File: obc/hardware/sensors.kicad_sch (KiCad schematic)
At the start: 6 parts, among them J5 Conn_Coaxial, U4 MAX-M10S, U6 MS5607-02BA

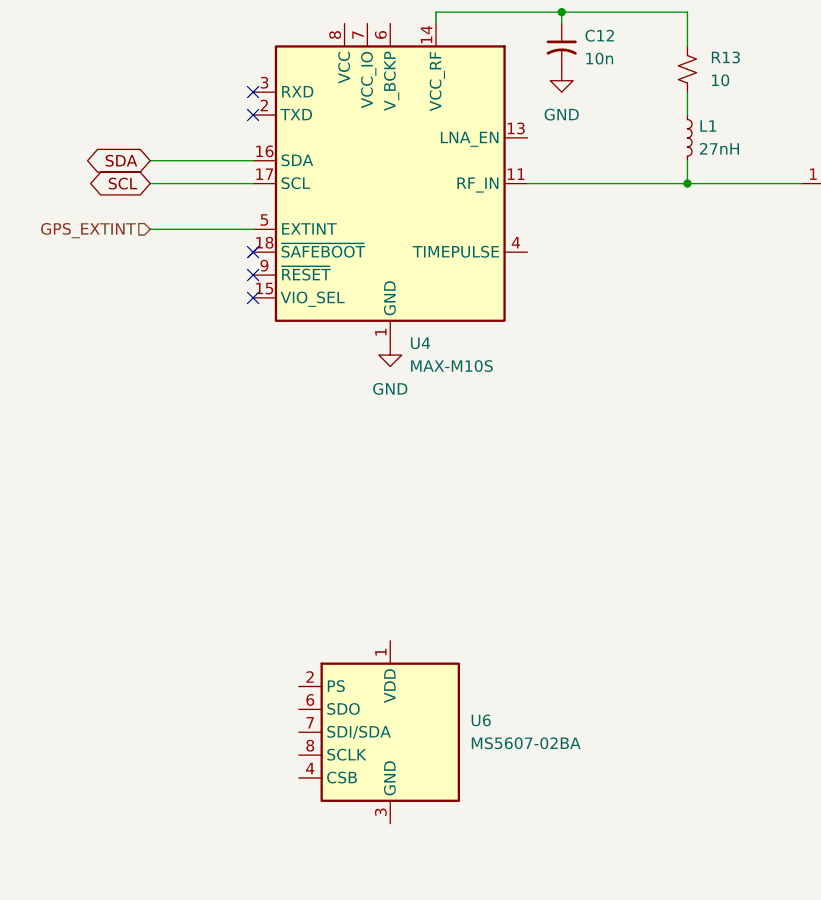
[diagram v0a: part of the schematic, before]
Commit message: added CAN, UART, supervisor, USB, power OR-ing, GPS, did layout
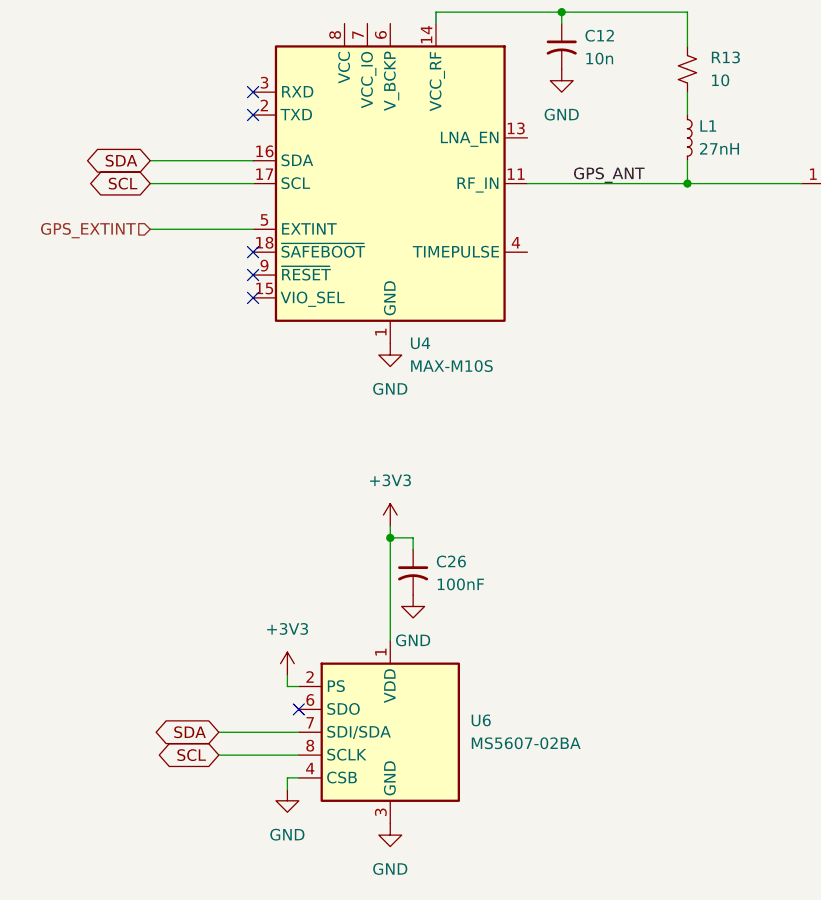
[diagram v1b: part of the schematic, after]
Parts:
- added C26: 100nF, Capacitor_SMD:C_0402_1005Metric, symbol Device:C_Small_US
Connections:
- net GND: now also U6.3 (GND), U6.4 (CSB), U6.5 (CSB), C26.2
- net SCL: now also U6.8 (SCLK)
- net SDA: now also U6.7 (SDI/SDA)
- net GPS_ANT: now reaches J5.1 (In), L1.2, U4.11 (RF_IN)
- net +3V3: now reaches U6.1 (VDD)
- net +3V3: now also U6.2 (PS), C26.1
- no-connect marks 5 -> 6

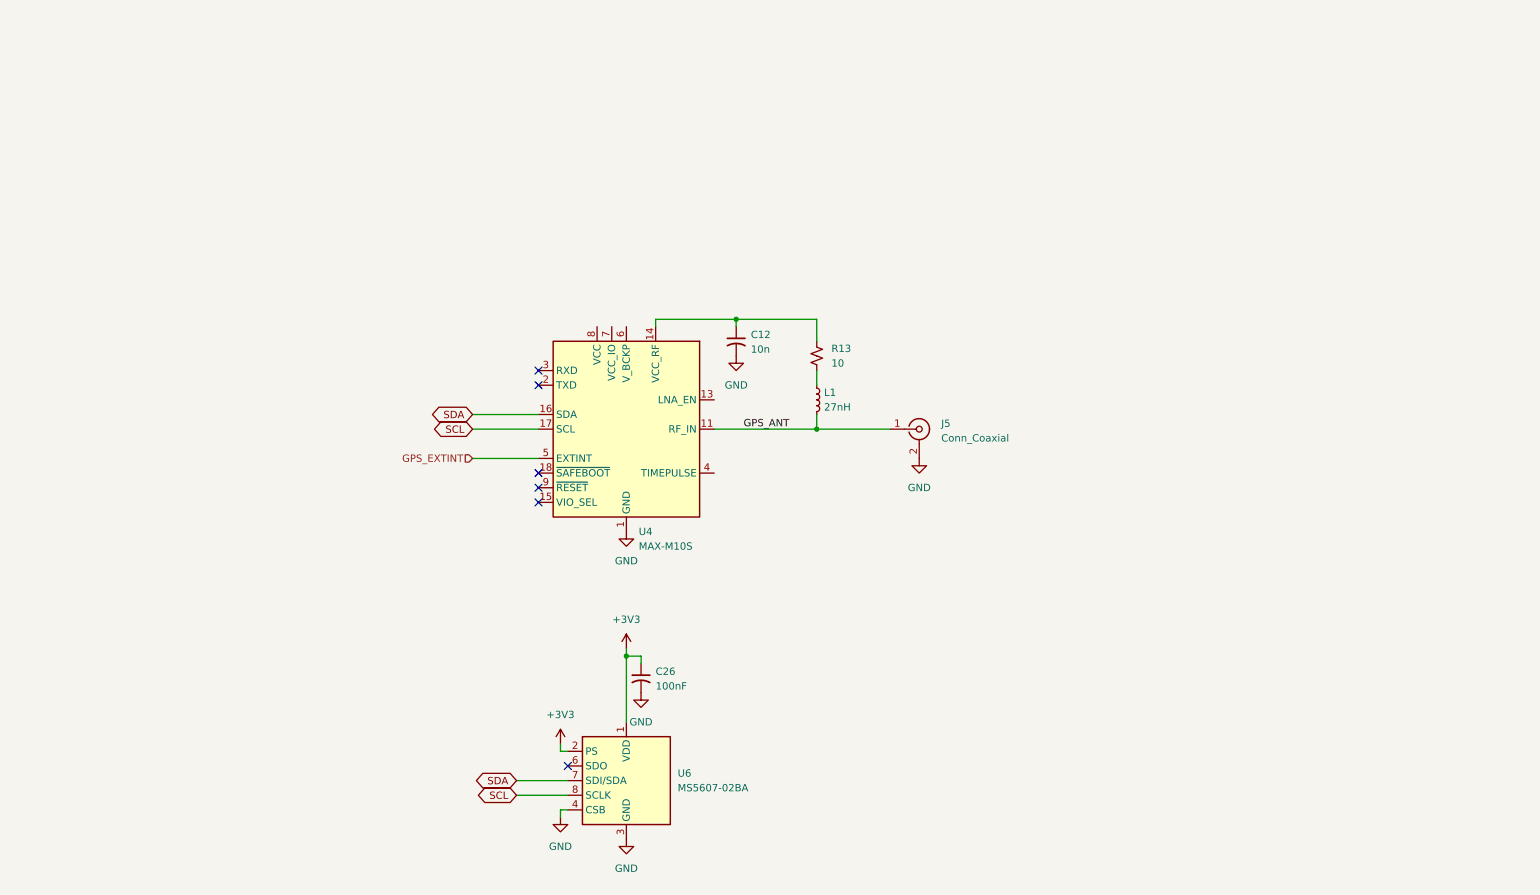
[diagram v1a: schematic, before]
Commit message: add SCRT and OSU AIAA logos, add IMU, add PPS LED, hook up some IOs
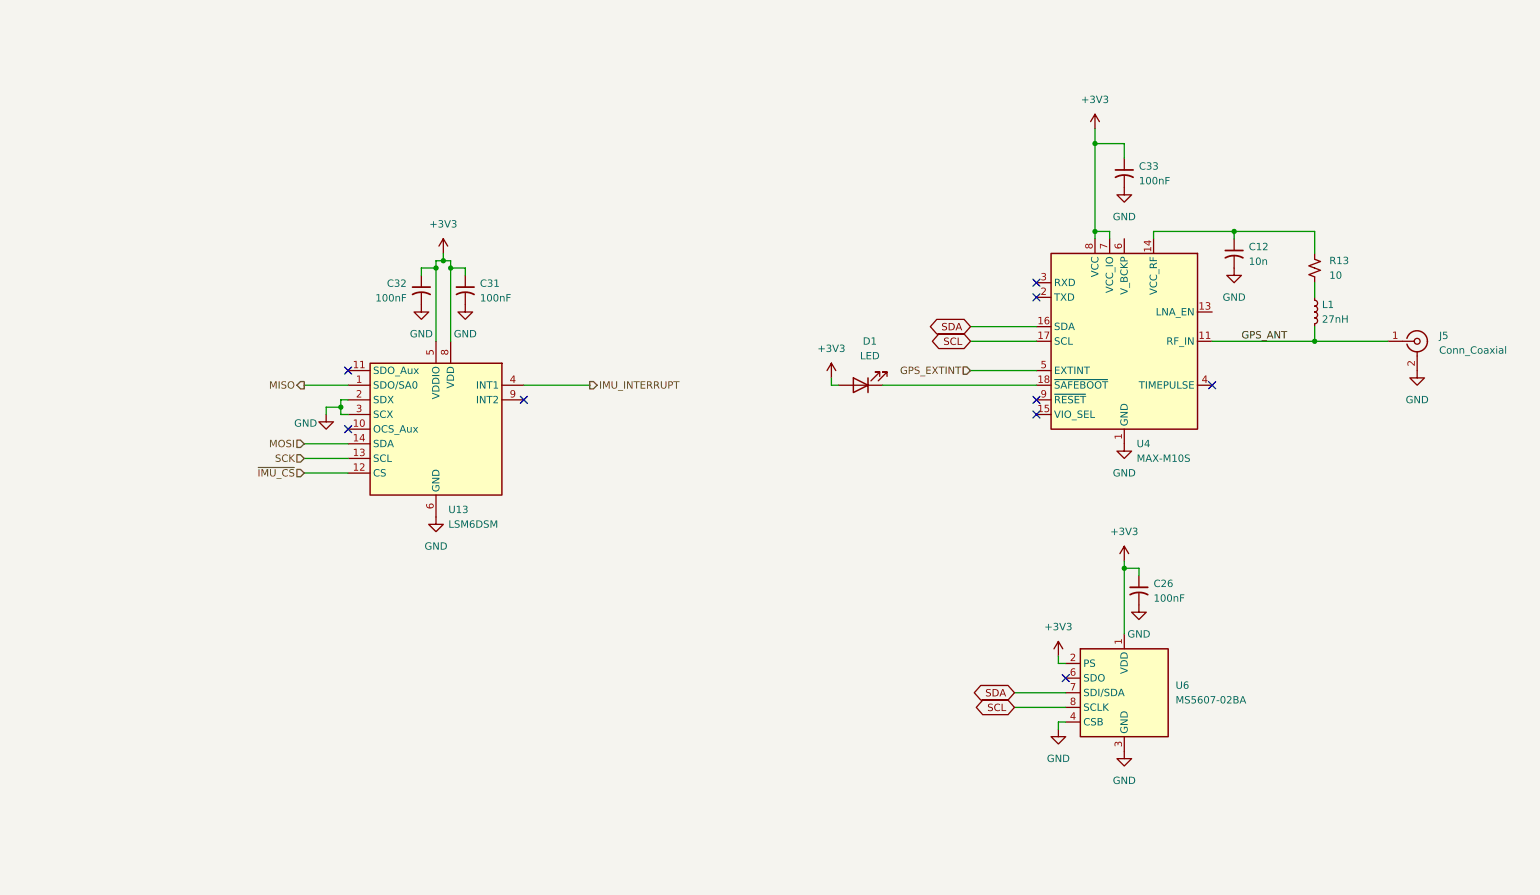
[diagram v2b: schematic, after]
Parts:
- added C31, C32, C33: 100nF, Capacitor_SMD:C_0402_1005Metric, symbol Device:C_Small_US
- added D1: LED, LED_SMD:LED_0805_2012Metric, symbol Device:LED
- added U13: LSM6DSM, Package_LGA:LGA-14_3x2.5mm_P0.5mm_LayoutBorder3x4y, symbol Sensor_Motion:LSM6DSM
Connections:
- net +3V3: now also U4.7 (VCC_IO), U4.8 (VCC), C31.1, C32.1, C33.1, D1.2 (A), U13.5 (VDDIO), U13.8 (VDD)
- net GND: now also C31.2, C32.2, C33.2, U13.2 (SDX), U13.3 (SCX), U13.6 (GND), U13.7 (GND)
- net at U4.18 (~{SAFEBOOT}): now also D1.1 (K)
- new net IMU_INTERRUPT: U13.4 (INT1)
- new net MISO: U13.1 (SDO/SA0)
- new net MOSI: U13.14 (SDA)
- new net SCK: U13.13 (SCL)
- new net ~{IMU_CS}: U13.12 (CS)
- no-connect marks 6 -> 9
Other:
- moved on the sheet: C12, C26, J5, L1, R13, U4, U6

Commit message: add antenna supervisor, ESD, reroute some stuff
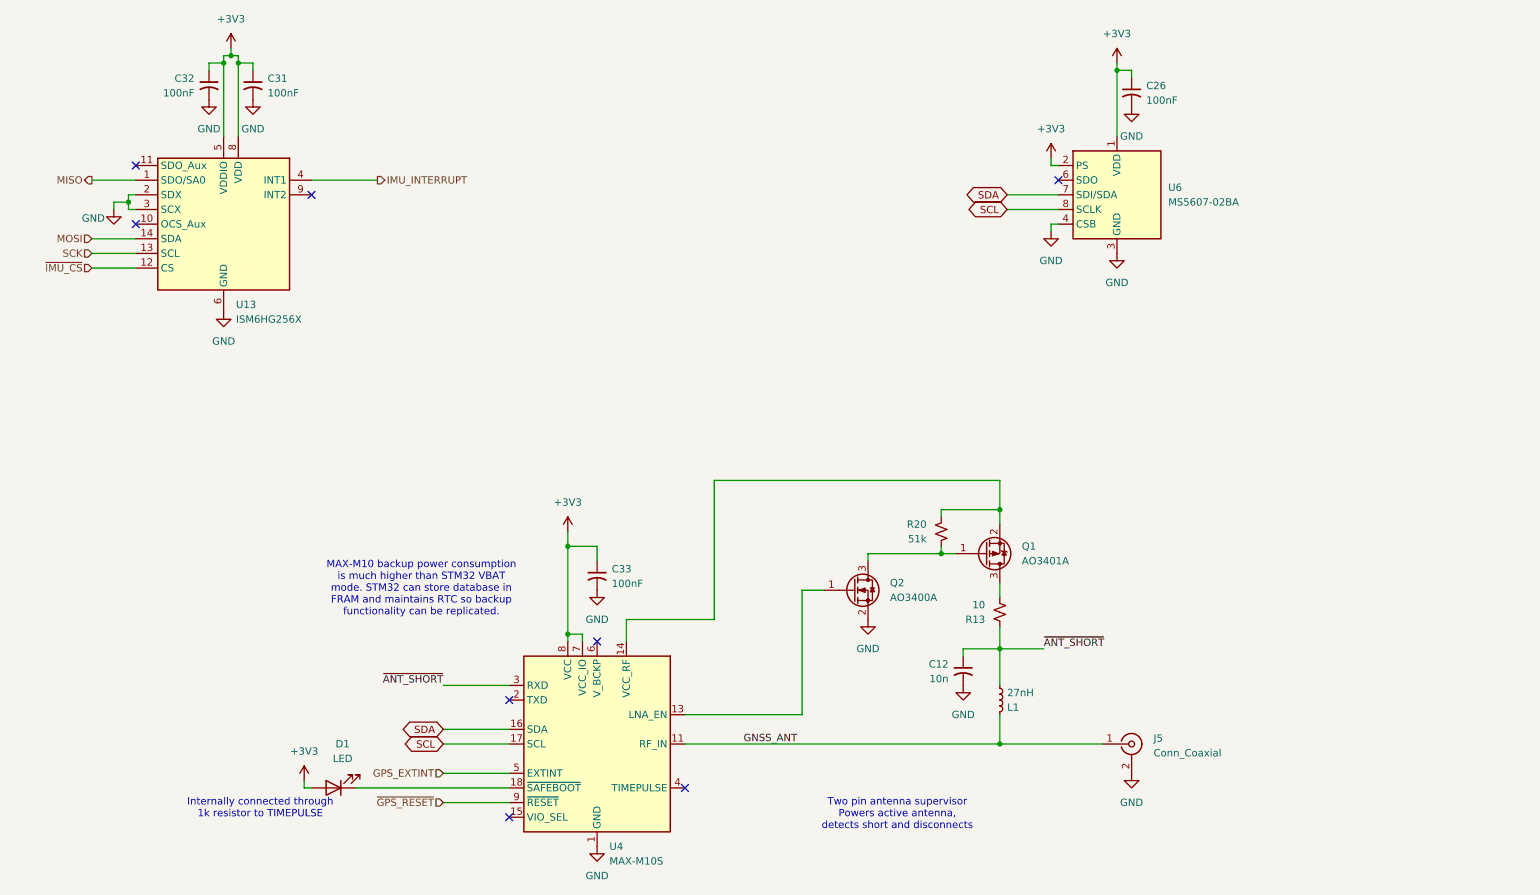
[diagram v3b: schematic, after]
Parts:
- added Q1: AO3401A, Package_TO_SOT_SMD:SOT-23, symbol Transistor_FET:AO3401A
- added Q2: AO3400A, Package_TO_SOT_SMD:SOT-23, symbol Transistor_FET:AO3400A
- added R20: 51k, Resistor_SMD:R_0402_1005Metric, symbol Device:R_Small_US
- U13: value LSM6DSM -> ISM6HG256X
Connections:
- net GND: now also Q2.2 (S)
- net at U4.13 (LNA_EN): now also Q2.1 (G)
- net ~{ANT_SHORT}: now reaches C12.1, R13.2
- net ~{ANT_SHORT}: now also L1.2, U4.3 (RXD); no longer U4.14 (VCC_RF)
- net ~{GPS_RESET}: now reaches U4.9 (~{RESET})
- net at R13.1: now also Q1.3 (D); no longer L1.1
- net GPS_ANT renamed GNSS_ANT
- net GNSS_ANT: now also L1.1; no longer L1.2
- new net: Q1.2 (S), R20.1, U4.14 (VCC_RF)
- new net: Q1.1 (G), Q2.3 (D), R20.2
- no-connect marks 9 -> 8
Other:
- note added: "Internally connected through 1k resistor to TIMEPULSE"
- note added: "MAX-M10 backup power consumption is much higher than STM32 VBAT mode. STM32 can store database in FRAM and maintains RTC so backup functionality can be replicated."
- note added: "Two pin antenna supervisor Powers active antenna, detects short and disconnects"
- moved on the sheet: C26, C31, C32, C33, D1, U13, U4, U6

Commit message: cleanup
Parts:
- C12: value 10n -> 10nF; LCSC (none) -> C15195
- C26, C31, C32, C33: LCSC (none) -> C1525
- D1: LCSC (none) -> C2297
- J5: LCSC (none) -> C88374
- L1: LCSC (none) -> C12669
- Q1: LCSC (none) -> C15127
- Q2: LCSC (none) -> C20917
- R13: LCSC (none) -> C17903
- R20: LCSC (none) -> C25794
- U4: LCSC (none) -> C4153167
- U6: LCSC (none) -> C97627

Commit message: add user LEDs, fix silkscreen
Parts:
- D1: LCSC C2297 -> C34499
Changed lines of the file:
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@@
 			)
 		)
-		(property "LCSC" "C2297"
+		(property "LCSC" "C34499"
 			(at 68.58 154.94 0)
 			(hide yes)

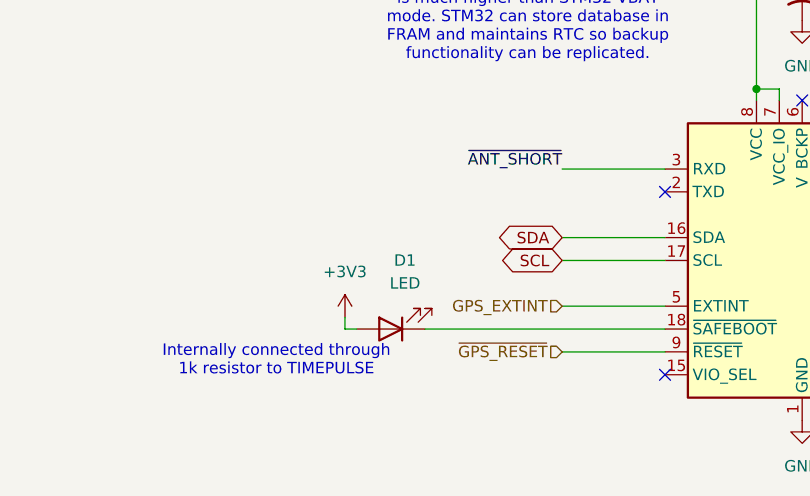
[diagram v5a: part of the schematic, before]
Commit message: LED part numbers
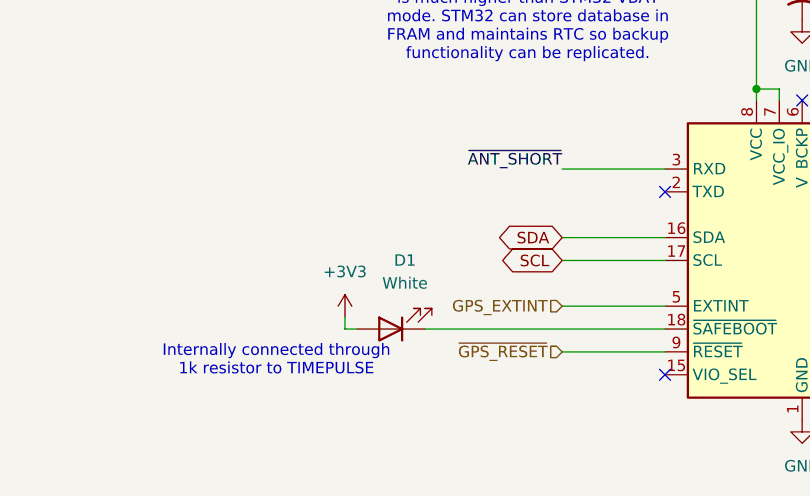
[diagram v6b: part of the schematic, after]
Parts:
- D1: value LED -> White
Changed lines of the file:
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@@
 			)
 		)
-		(property "Value" "LED"
+		(property "Value" "White"
 			(at 70.1675 149.86 0)
 			(show_name no)

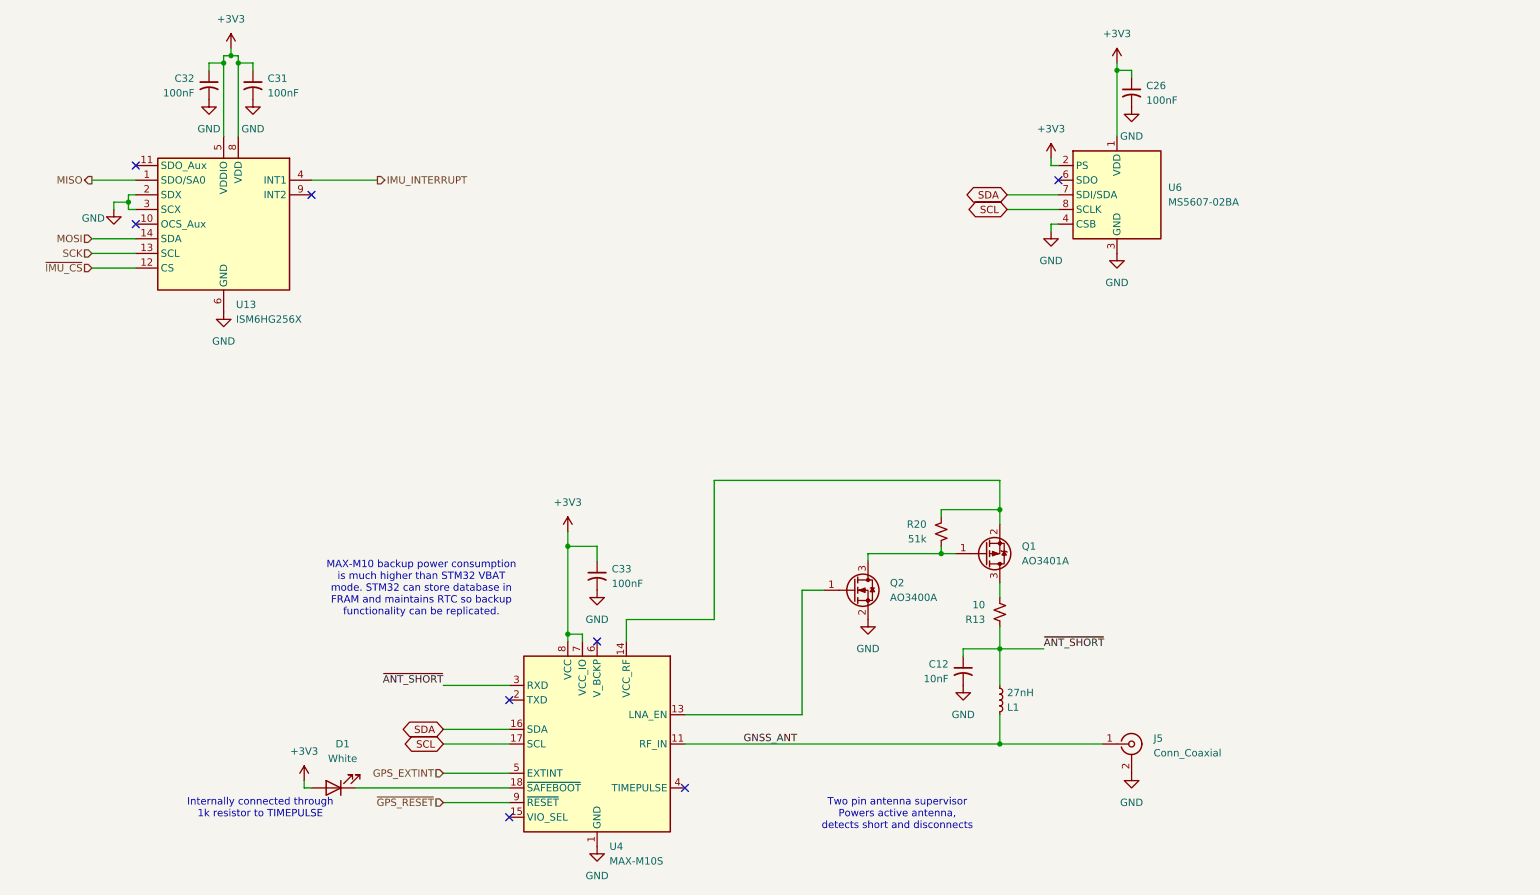
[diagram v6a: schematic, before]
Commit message: DNP parts that JLC shouldn't assemble
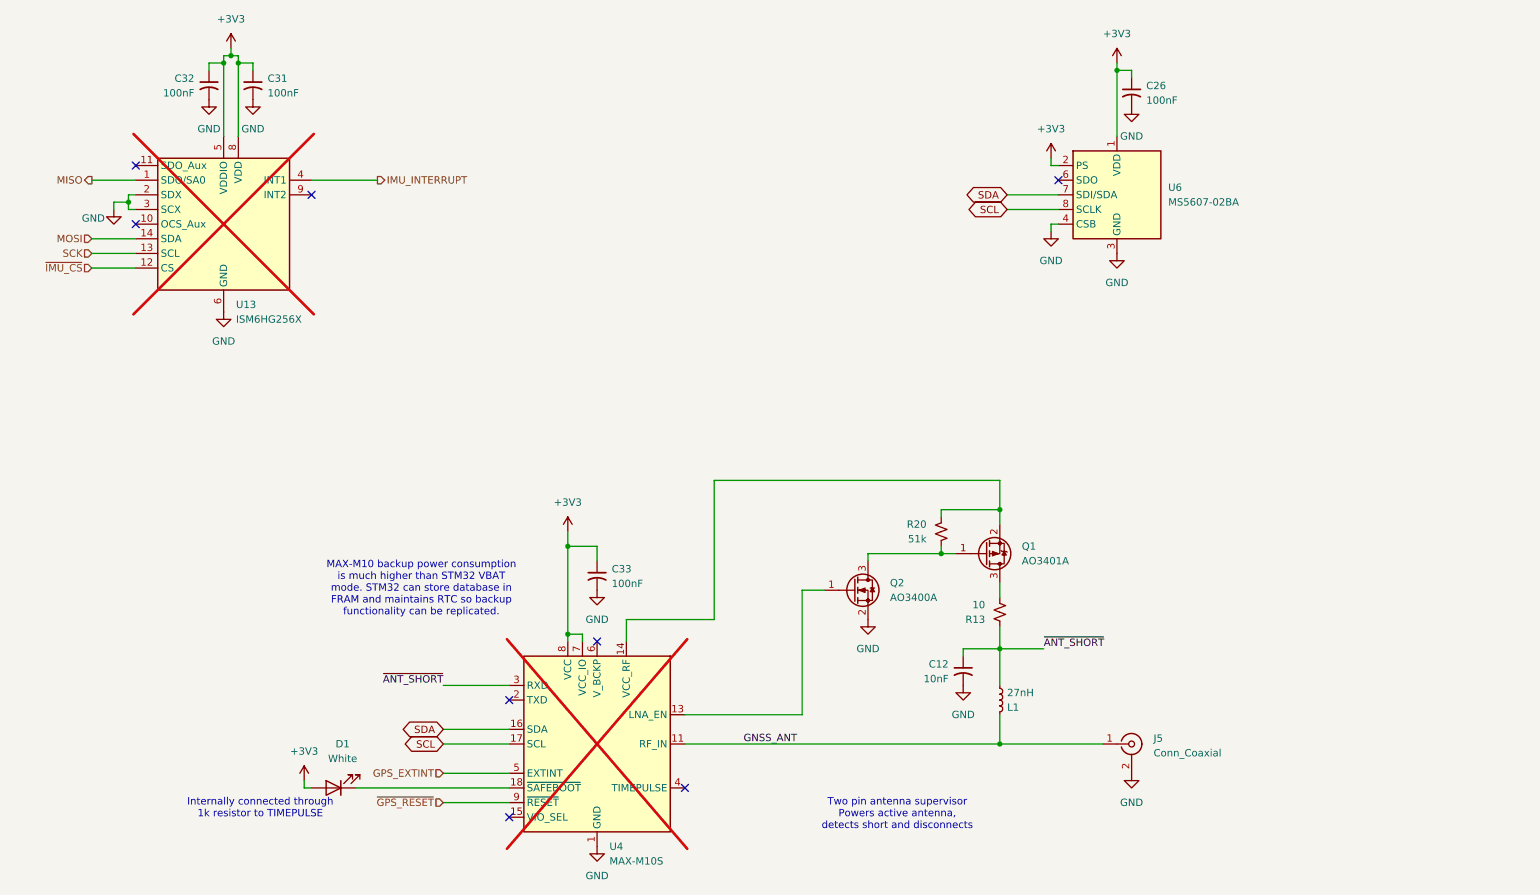
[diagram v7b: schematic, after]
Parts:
- U13, U4: now not fitted
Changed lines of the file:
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@@
 		(on_board yes)
 		(in_pos_files yes)
-		(dnp no)
+		(dnp yes)
 		(fields_autoplaced yes)
 		(property "Reference" "U4"
@@
 		(on_board yes)
 		(in_pos_files yes)
-		(dnp no)
+		(dnp yes)
 		(fields_autoplaced yes)
 		(property "Reference" "U13"
